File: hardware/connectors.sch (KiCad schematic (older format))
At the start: 17 parts, among them J201 DB15, J202 DB9, J203 DB9, P201 CONN_01X02, P202 CONN_01X08, P203 CONN_01X02, P204 CONN_01X02, P205 CONN_01X02, P206 CONN_01X02

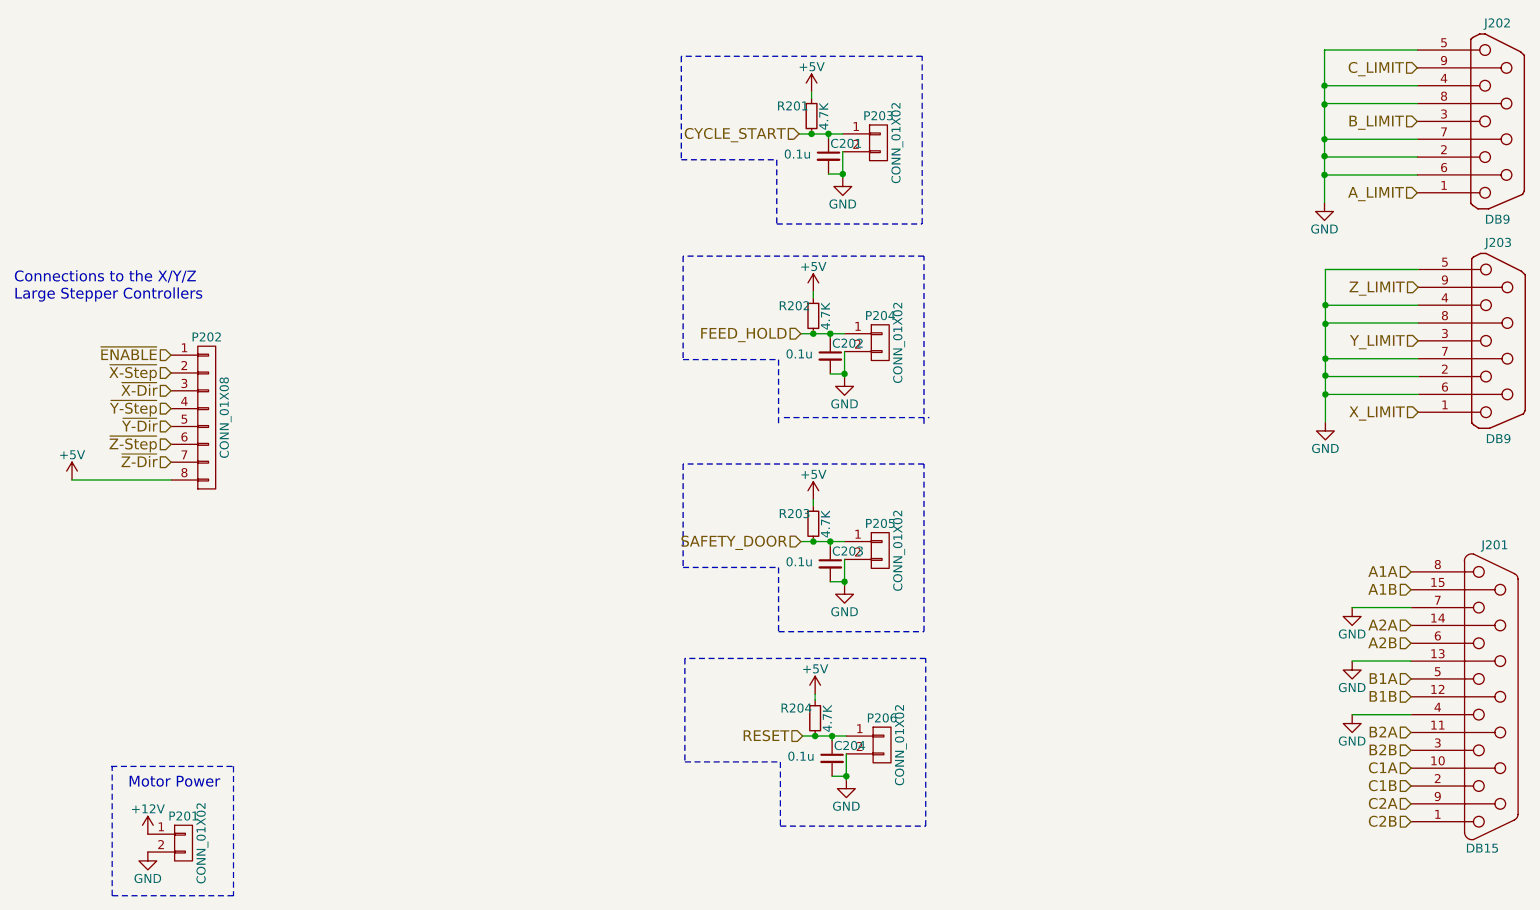
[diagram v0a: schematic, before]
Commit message: changed connector footprints and added rotory dip switch footprint
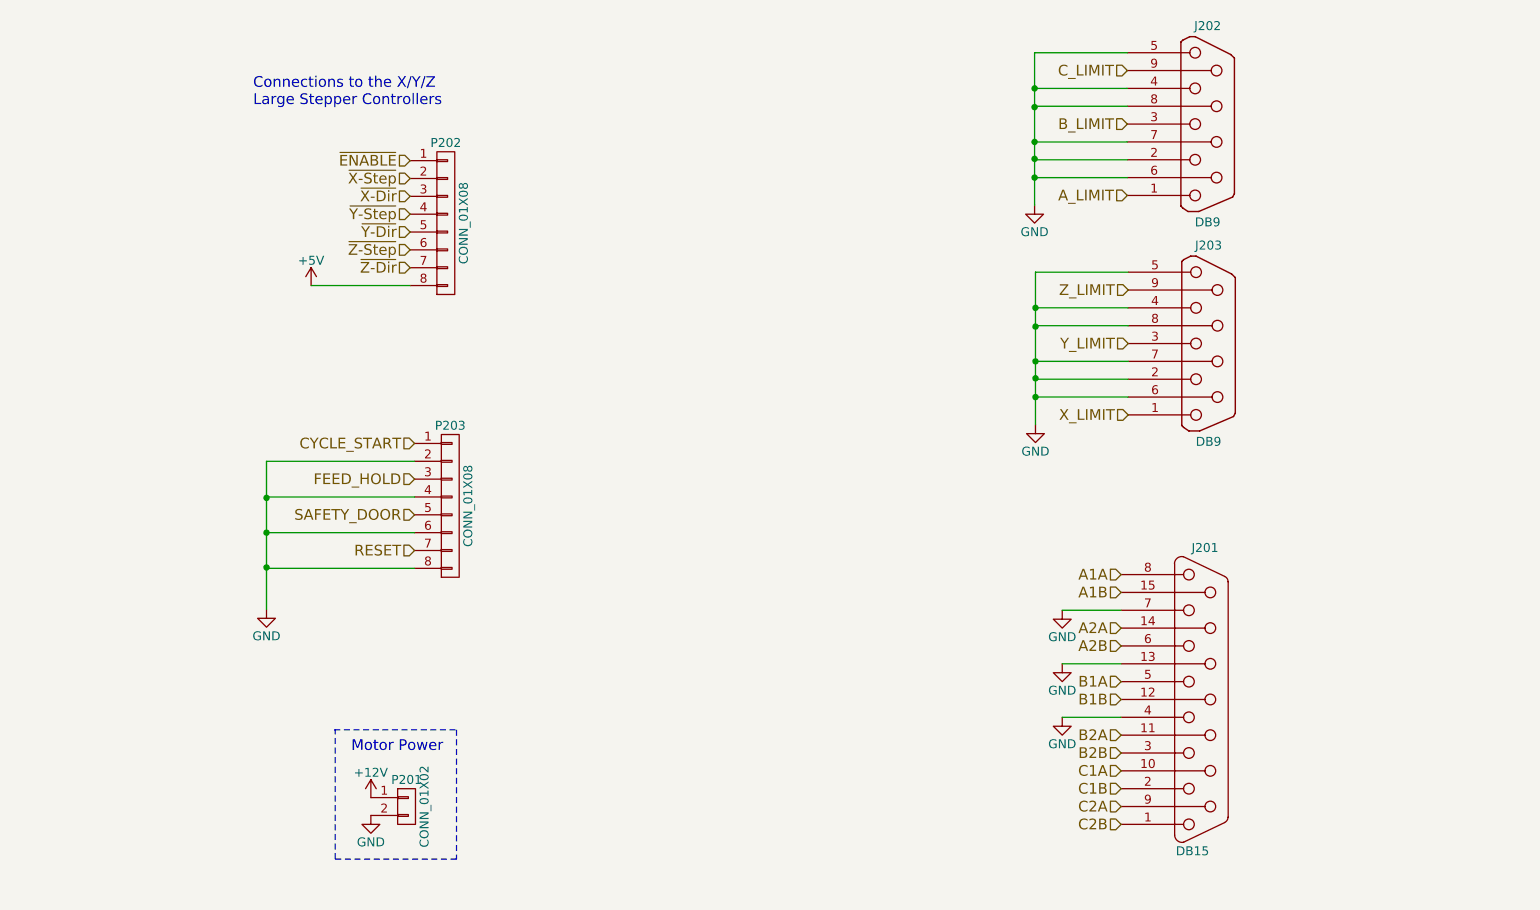
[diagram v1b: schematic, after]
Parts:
- removed C201, C202, C203, C204: 0.1u, Capacitors_SMD:C_0805_HandSoldering, symbol C_Small
- removed P203, P204, P205, P206: CONN_01X02, 6axis:Terminal_Block_200_mil, symbol CONN_01X02
- removed R201, R202, R203, R204: 4.7K, Resistors_SMD:R_0805_HandSoldering, symbol R_Small
- added P203: CONN_01X08, 6axis:Terminal_Block_200_mil_8pos, symbol CONN_01X08
- P201: Fieldname (none) -> Value; MPN (none) -> OSTTC022162
- P202: footprint Pin_Headers:Pin_Header_Straight_1x08 -> 6axis:Terminal_Block_200_mil_8pos; Fieldname (none) -> Value; MPN (none) -> OSTTC022162; Note (none) -> Combine multiples of 2-position terminal block
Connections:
- net CYCLE_START: now also P203.1 (P1)
- net FEED_HOLD: now also P203.3 (P3)
- net GND: now also P203.2 (P2), P203.4 (P4), P203.6 (P6), P203.8 (P8)
- net RESET: now also P203.7 (P7)
- net SAFETY_DOOR: now also P203.5 (P5)
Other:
- moved on the sheet: J201, J202, J203, P201, P202

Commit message: changed dsub connectors to horizontal
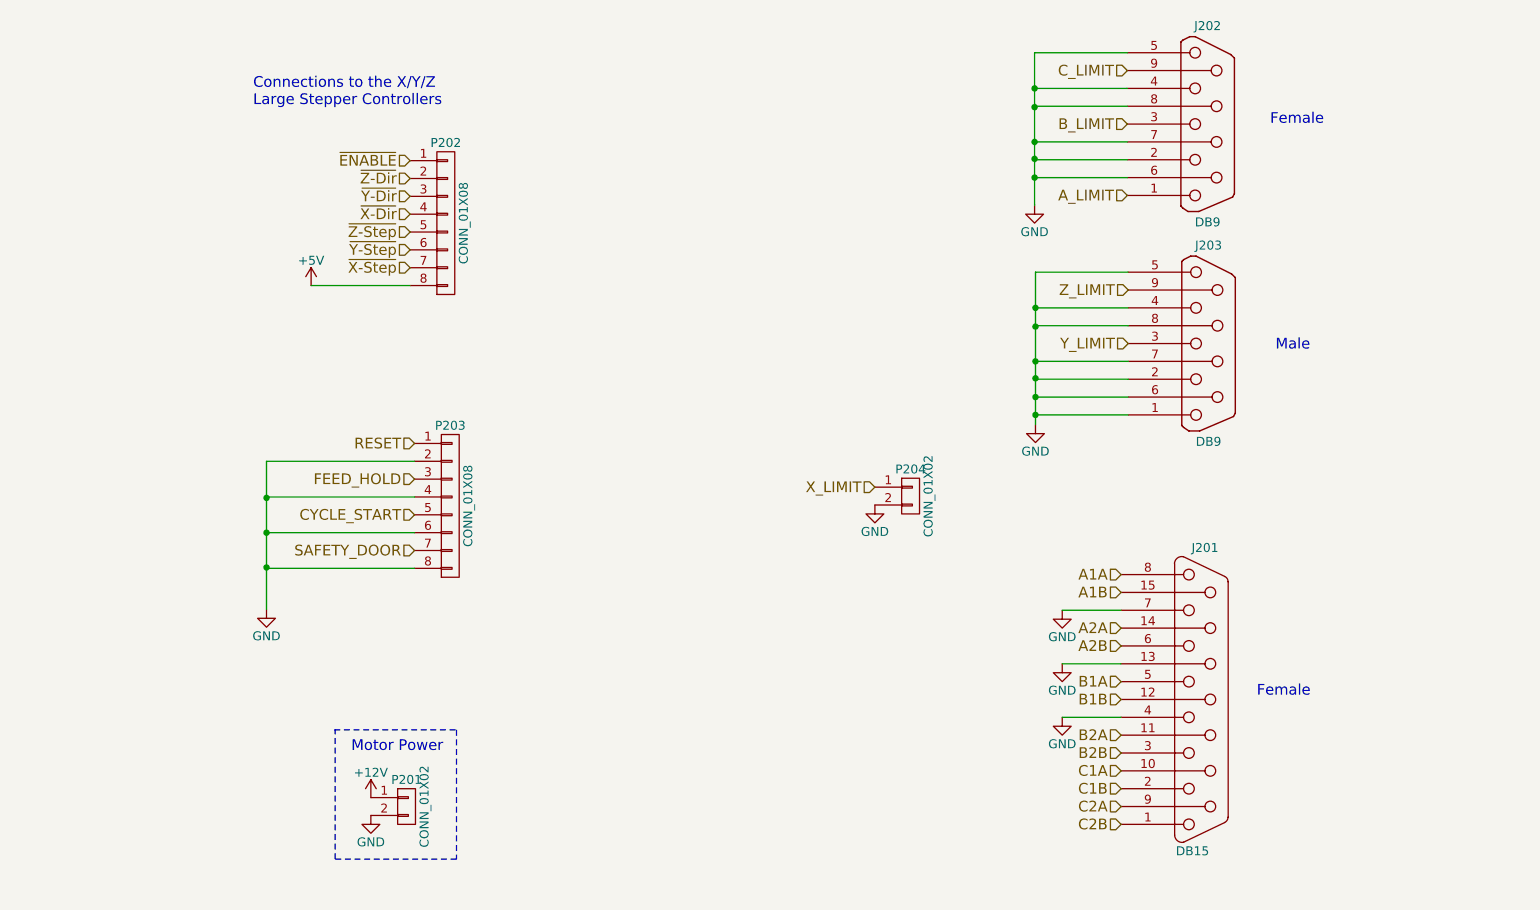
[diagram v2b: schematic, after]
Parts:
- added P204: CONN_01X02, 6axis:Terminal_Block_200_mil, symbol CONN_01X02
- J201: MPN D15S24A4GV00LF -> D15S33E4GV00LF
- J202: MPN D09S24A4GV00LF -> LD09S13A4GV00LF
- J203: MPN D09P24A4GV00LF -> LD09P13A4GX00LF
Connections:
- net CYCLE_START: now also P203.5 (P5); no longer P203.1 (P1)
- net GND: now also J203.1, P204.2 (P2)
- net RESET: now also P203.1 (P1); no longer P203.7 (P7)
- net SAFETY_DOOR: now also P203.7 (P7); no longer P203.5 (P5)
- net X_LIMIT: now also P204.1 (P1); no longer J203.1
- net ~X-Dir: now also P202.4 (P4); no longer P202.3 (P3)
- net ~X-Step: now also P202.7 (P7); no longer P202.2 (P2)
- net ~Y-Dir: now also P202.3 (P3); no longer P202.5 (P5)
- net ~Y-Step: now also P202.6 (P6); no longer P202.4 (P4)
- net ~Z-Dir: now also P202.2 (P2); no longer P202.7 (P7)
- net ~Z-Step: now also P202.5 (P5); no longer P202.6 (P6)
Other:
- note added: "Female"
- note added: "Male"
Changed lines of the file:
@@
 F 1 "DB9" H 8430 1250 50  0000 C CNN
 F 2 "Connectors:DB9FD" H 8430 1800 50  0001 C CNN
-F 3 "http://portal.fciconnect.com/Comergent//fci/drawing/c01-8646-0752.pdf" H 8430 1800 50  0001 C CNN
-F 4 "D09S24A4GV00LF" H 8430 1800 60  0001 C CNN "MPN"
-F 5 "Value" H 8430 1800 60  0001 C CNN "Fieldname"
+F 3 "http://portal.fciconnect.com/Comergent//fci/drawing/10130913.pdf" H 8430 1800 50  0001 C CNN
+F 4 "Value" H 8430 1800 60  0001 C CNN "Fieldname"
+F 5 "LD09S13A4GV00LF" H 8430 1800 60  0001 C CNN "MPN"
 	1    8430 1800
 	1    0    0    -1
@@
 F 1 "DB9" H 8435 2480 50  0000 C CNN
 F 2 "Connectors:DB9MD" H 8435 3030 50  0001 C CNN
-F 3 "http://portal.fciconnect.com/Comergent//fci/drawing/c01-8646-0816.pdf" H 8435 3030 50  0001 C CNN
-F 4 "D09P24A4GV00LF" H 8435 3030 60  0001 C CNN "MPN"
-F 5 "Value" H 8435 3030 60  0001 C CNN "Fieldname"
+F 3 "http://portal.fciconnect.com/Comergent//fci/drawing/10130913.pdf" H 8435 3030 50  0001 C CNN
+F 4 "Value" H 8435 3030 60  0001 C CNN "Fieldname"
+F 5 "LD09P13A4GX00LF" H 8435 3030 60  0001 C CNN "MPN"
 	1    8435 3030
 	1    0    0    -1
@@
 F 1 "DB15" H 8345 4175 50  0000 C CNN
 F 2 "Connectors:DB15FD" H 8395 5025 50  0001 C CNN
-F 3 "http://portal.fciconnect.com/Comergent//fci/drawing/c01-8646-0752.pdf" H 8395 5025 50  0001 C CNN
-F 4 "D15S24A4GV00LF" H 8395 5025 60  0001 C CNN "MPN"
-F 5 "Value" H 8395 5025 60  0001 C CNN "Fieldname"
+F 3 "http://portal.fciconnect.com/Comergent//fci/drawing/c01-8646-0824.pdf" H 8395 5025 50  0001 C CNN
+F 4 "Value" H 8395 5025 60  0001 C CNN "Fieldname"
+F 5 "D15S33E4GV00LF" H 8395 5025 60  0001 C CNN "MPN"
 	1    8395 5025
 	1    0    0    -1
@@
 Text HLabel 3960 2005 0    60   Input ~ 0
 ~ENABLE
-Text HLabel 3960 2105 0    60   Input ~ 0
+Text HLabel 3960 2605 0    60   Input ~ 0
 ~X-Step
-Text HLabel 3960 2205 0    60   Input ~ 0
+Text HLabel 3960 2305 0    60   Input ~ 0
 ~X-Dir
 $Comp
@@
 	1    0    0    -1
 $EndComp
-Text HLabel 3960 2305 0    60   Input ~ 0
+Text HLabel 3960 2505 0    60   Input ~ 0
 ~Y-Step
+Text HLabel 3960 2205 0    60   Input ~ 0
+~Y-Dir
 Text HLabel 3960 2405 0    60   Input ~ 0
-~Y-Dir
-Text HLabel 3960 2505 0    60   Input ~ 0
 ~Z-Step
-Text HLabel 3960 2605 0    60   Input ~ 0
+Text HLabel 3960 2105 0    60   Input ~ 0
 ~Z-Dir
 Wire Wire Line
@@
 	1    0    0    -1
 $EndComp
-Text HLabel 3985 3590 0    60   Input ~ 0
+Text HLabel 3985 3990 0    60   Input ~ 0
 CYCLE_START
 Text HLabel 3985 3790 0    60   Input ~ 0
 FEED_HOLD
-Text HLabel 3985 3990 0    60   Input ~ 0
+Text HLabel 3985 4190 0    60   Input ~ 0
 SAFETY_DOOR
-Text HLabel 3985 4190 0    60   Input ~ 0
+Text HLabel 3985 3590 0    60   Input ~ 0
 RESET
 Text HLabel 7980 1500 0    60   Input ~ 0
@@
 Text HLabel 7985 3030 0    60   Input ~ 0
 Y_LIMIT
-Text HLabel 7985 3430 0    60   Input ~ 0
+Text HLabel 6565 3835 0    60   Input ~ 0
 X_LIMIT
 Text HLabel 7945 4325 0    60   Input ~ 0
@@
 	3155 4290 3155 4285
 Connection ~ 3155 4285
+$Comp
+L CONN_01X02 P204
+U 1 1 59A0B645
+P 6765 3885
+F 0 "P204" H 6765 4035 50  0000 C CNN
+F 1 "CONN_01X02" V 6865 3885 50  0000 C CNN
+F 2 "6axis:Terminal_Block_200_mil" H 6765 3885 50  0001 C CNN
+F 3 "http://www.on-shore.com/wp-content/uploads/2015/09/osttcxx2162.pdf" H 6765 3885 50  0001 C CNN
+F 4 "OSTTC022162" H 6765 3885 60  0001 C CNN "MPN"
+F 5 "Value" H 6765 3885 60  0001 C CNN "Fieldname"
+	1    6765 3885
+	1    0    0    -1
+$EndComp
+$Comp
+L GND #PWR037
+U 1 1 59A0B64B
+P 6565 3935
+F 0 "#PWR037" H 6565 3685 50  0001 C CNN
+F 1 "GND" H 6565 3785 50  0000 C CNN
+F 2 "" H 6565 3935 50  0000 C CNN
+F 3 "" H 6565 3935 50  0000 C CNN
+	1    6565 3935
+	1    0    0    -1
+$EndComp
+Wire Wire Line
+	7985 3430 7465 3430
+Connection ~ 7465 3430
+Text Notes 8705 5015 0    60   ~ 0
+Female
+Text Notes 8810 3075 0    60   ~ 0
+Male
+Text Notes 8780 1810 0    60   ~ 0
+Female
 $EndSCHEMATC

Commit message: completed board and generated gerbers
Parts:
- J201: footprint Connectors:DB15FD -> 6axis:D15S33E4GV00LF
- J202: footprint Connectors:DB9FD -> 6axis:LD09S33E4GV00LF; MPN LD09S13A4GV00LF -> LD09S33E4GV00LF
- J203: footprint Connectors:DB9MD -> 6axis:LD09P33E4GV00LF; MPN LD09P13A4GX00LF -> LD09P33E4GV00LF
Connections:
- net A1A: now also J201.15 (P15); no longer J201.8
- net A1B: now also J201.7; no longer J201.15 (P15)
- net A2A: now also J201.6; no longer J201.14 (P14)
- net A2B: now also J201.14 (P14); no longer J201.6
- net B1A: now also J201.12 (P12); no longer J201.5
- net B1B: now also J201.4; no longer J201.12 (P12)
- net B2A: now also J201.3; no longer J201.11 (P111)
- net B2B: now also J201.11 (P111); no longer J201.3
- net C1A: now also J201.1; no longer J201.10 (P10)
- net C2A: now also J201.10 (P10); no longer J201.9 (P9)
- net C2B: now also J201.9 (P9); no longer J201.1
- net GND: now also J201.5, J201.8; no longer J201.4, J201.7
- net ~X-Dir: now also P202.3 (P3); no longer P202.4 (P4)
- net ~X-Step: now also P202.6 (P6); no longer P202.7 (P7)
- net ~Y-Dir: now also P202.4 (P4); no longer P202.3 (P3)
- net ~Y-Step: now also P202.7 (P7); no longer P202.6 (P6)
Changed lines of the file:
@@
 F 0 "J202" H 8430 2350 50  0000 C CNN
 F 1 "DB9" H 8430 1250 50  0000 C CNN
-F 2 "Connectors:DB9FD" H 8430 1800 50  0001 C CNN
-F 3 "http://portal.fciconnect.com/Comergent//fci/drawing/10130913.pdf" H 8430 1800 50  0001 C CNN
+F 2 "6axis:LD09S33E4GV00LF" H 8430 1800 50  0001 C CNN
+F 3 "http://portal.fciconnect.com/Comergent//fci/drawing/10130914.pdf" H 8430 1800 50  0001 C CNN
 F 4 "Value" H 8430 1800 60  0001 C CNN "Fieldname"
-F 5 "LD09S13A4GV00LF" H 8430 1800 60  0001 C CNN "MPN"
+F 5 "LD09S33E4GV00LF" H 8430 1800 60  0001 C CNN "MPN"
 	1    8430 1800
 	1    0    0    -1
@@
 F 0 "J203" H 8435 3580 50  0000 C CNN
 F 1 "DB9" H 8435 2480 50  0000 C CNN
-F 2 "Connectors:DB9MD" H 8435 3030 50  0001 C CNN
-F 3 "http://portal.fciconnect.com/Comergent//fci/drawing/10130913.pdf" H 8435 3030 50  0001 C CNN
+F 2 "6axis:LD09P33E4GV00LF" H 8435 3030 50  0001 C CNN
+F 3 "http://portal.fciconnect.com/Comergent//fci/drawing/10130914.pdf" H 8435 3030 50  0001 C CNN
 F 4 "Value" H 8435 3030 60  0001 C CNN "Fieldname"
-F 5 "LD09P13A4GX00LF" H 8435 3030 60  0001 C CNN "MPN"
+F 5 "LD09P33E4GV00LF" H 8435 3030 60  0001 C CNN "MPN"
 	1    8435 3030
 	1    0    0    -1
@@
 F 0 "J201" H 8415 5875 50  0000 C CNN
 F 1 "DB15" H 8345 4175 50  0000 C CNN
-F 2 "Connectors:DB15FD" H 8395 5025 50  0001 C CNN
+F 2 "6axis:D15S33E4GV00LF" H 8395 5025 50  0001 C CNN
 F 3 "http://portal.fciconnect.com/Comergent//fci/drawing/c01-8646-0824.pdf" H 8395 5025 50  0001 C CNN
 F 4 "Value" H 8395 5025 60  0001 C CNN "Fieldname"
@@
 L GND #PWR032
 U 1 1 599D91FC
-P 7615 4525
-F 0 "#PWR032" H 7615 4275 50  0001 C CNN
-F 1 "GND" H 7615 4375 50  0000 C CNN
-F 2 "" H 7615 4525 50  0000 C CNN
-F 3 "" H 7615 4525 50  0000 C CNN
-	1    7615 4525
-	1    0    0    -1
-$EndComp
-Wire Wire Line
-	7945 4525 7615 4525
+P 7615 4325
+F 0 "#PWR032" H 7615 4075 50  0001 C CNN
+F 1 "GND" H 7615 4175 50  0000 C CNN
+F 2 "" H 7615 4325 50  0000 C CNN
+F 3 "" H 7615 4325 50  0000 C CNN
+	1    7615 4325
+	1    0    0    -1
+$EndComp
+Wire Wire Line
+	7945 4325 7615 4325
 $Comp
 L GND #PWR033
@@
 Wire Wire Line
 	7945 4825 7615 4825
-$Comp
-L GND #PWR034
-U 1 1 599D920A
-P 7615 5125
-F 0 "#PWR034" H 7615 4875 50  0001 C CNN
-F 1 "GND" H 7615 4975 50  0000 C CNN
-F 2 "" H 7615 5125 50  0000 C CNN
-F 3 "" H 7615 5125 50  0000 C CNN
-	1    7615 5125
-	1    0    0    -1
-$EndComp
-Wire Wire Line
-	7945 5125 7615 5125
 Text HLabel 3960 2005 0    60   Input ~ 0
 ~ENABLE
-Text HLabel 3960 2605 0    60   Input ~ 0
+Text HLabel 3960 2505 0    60   Input ~ 0
 ~X-Step
-Text HLabel 3960 2305 0    60   Input ~ 0
+Text HLabel 3960 2205 0    60   Input ~ 0
 ~X-Dir
 $Comp
@@
 	1    0    0    -1
 $EndComp
-Text HLabel 3960 2505 0    60   Input ~ 0
+Text HLabel 3960 2605 0    60   Input ~ 0
 ~Y-Step
-Text HLabel 3960 2205 0    60   Input ~ 0
+Text HLabel 3960 2305 0    60   Input ~ 0
 ~Y-Dir
 Text HLabel 3960 2405 0    60   Input ~ 0
@@
 Text HLabel 6565 3835 0    60   Input ~ 0
 X_LIMIT
-Text HLabel 7945 4325 0    60   Input ~ 0
+Text HLabel 7945 4425 0    60   Input ~ 0
 A1A
-Text HLabel 7945 4425 0    60   Input ~ 0
+Text HLabel 7945 4525 0    60   Input ~ 0
 A1B
+Text HLabel 7945 4725 0    60   Input ~ 0
+A2A
 Text HLabel 7945 4625 0    60   Input ~ 0
-A2A
-Text HLabel 7945 4725 0    60   Input ~ 0
 A2B
-Text HLabel 7945 4925 0    60   Input ~ 0
+Text HLabel 7945 5025 0    60   Input ~ 0
 B1A
-Text HLabel 7945 5025 0    60   Input ~ 0
+Text HLabel 7945 5125 0    60   Input ~ 0
 B1B
+Text HLabel 7945 5325 0    60   Input ~ 0
+B2A
 Text HLabel 7945 5225 0    60   Input ~ 0
-B2A
-Text HLabel 7945 5325 0    60   Input ~ 0
 B2B
-Text HLabel 7945 5425 0    60   Input ~ 0
+Text HLabel 7945 5725 0    60   Input ~ 0
 C1A
 Text HLabel 7945 5525 0    60   Input ~ 0
 C1B
+Text HLabel 7945 5425 0    60   Input ~ 0
+C2A
 Text HLabel 7945 5625 0    60   Input ~ 0
-C2A
-Text HLabel 7945 5725 0    60   Input ~ 0
 C2B
 $Comp
@@
 Text Notes 8780 1810 0    60   ~ 0
 Female
+Wire Wire Line
+	7830 4925 7945 4925
+Wire Wire Line
+	7830 4925 7830 4825
+Connection ~ 7830 4825
 $EndSCHEMATC
